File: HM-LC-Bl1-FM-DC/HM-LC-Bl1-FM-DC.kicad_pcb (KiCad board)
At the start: 2 copper layers, 53.1 x 26.9 mm, 32 parts, among them J2 FTDI, J4 Reset, K1 OMRONG6S-2, K2 OMRONG6S-2, Q1 BC817, Q2 BC817, SW2 Config, U1 ATMEGA328P-AU, U2 CC1101, U3 AM1S-2403S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

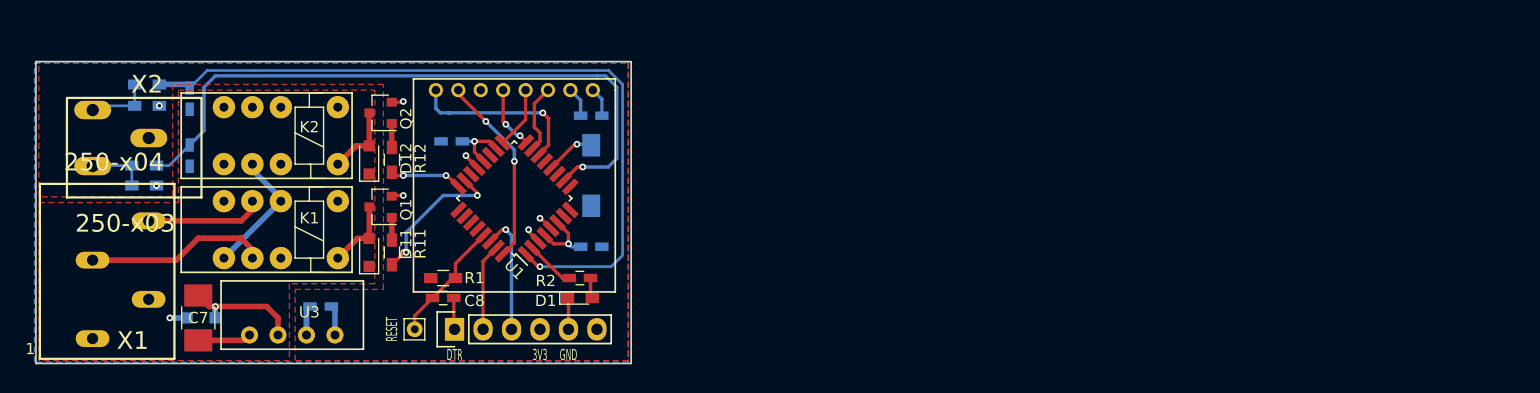
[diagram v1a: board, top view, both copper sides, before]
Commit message: basic routing finished
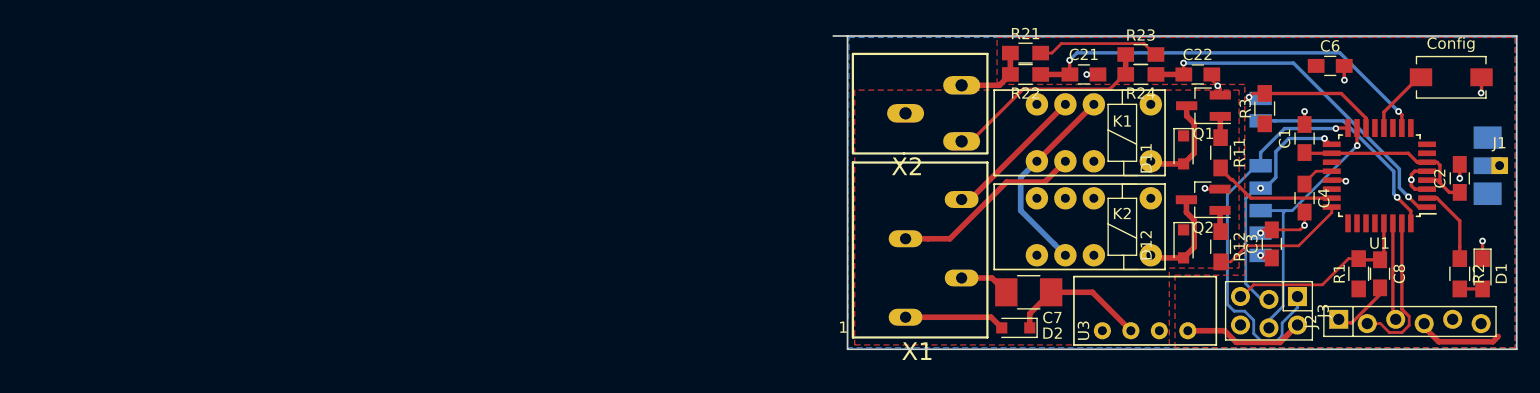
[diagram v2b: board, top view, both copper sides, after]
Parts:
- removed J4: Reset, Connectors:Pin_d0.7mm_L6.5mm_W1.8mm_FlatFork
- added C4: 100n, Capacitors_SMD:C_0805_HandSoldering, F.Cu at (181.1, 99.7)
- added J1: Conn_01x01, Measurement_Points:Measurement_Point_Square-TH_Small, F.Cu at (198.5, 96.8)
- added J3: ISP, myPinHeaders:Pin_Header_Straight_2x03_Pitch2.54mm_Tight_Fit, F.Cu at (180.5, 108.5)
- added R3: 10k, Resistors_SMD:R_0805_HandSoldering, F.Cu at (177.5, 91.7)
- C1, C2, C21, C22, C6: footprint Capacitors_SMD:C_0603_HandSoldering -> Capacitors_SMD:C_0805_HandSoldering; moved to F.Cu
- C3: value 100n -> 1u; footprint Capacitors_SMD:C_0603_HandSoldering -> Capacitors_SMD:C_0805_HandSoldering; moved to F.Cu
- C8: footprint Capacitors_SMD:C_0603_HandSoldering -> Capacitors_SMD:C_0805_HandSoldering
- D1: footprint LEDs:LED_0603_HandSoldering -> LEDs:LED_0805_HandSoldering
- D2, SW2: moved to F.Cu
- J2: value FTDI -> FtdiConnector; footprint Pin_Headers:Pin_Header_Straight_1x06 -> myPinHeaders:Pin_Header_Straight_1x06_Pitch2.54mm_Tight_Fit
- K1, K2: footprint Relay_mod:Relay_Omron_G6S-2 -> myRelais:Relay_Omron_G6S-2
- Q1, Q2: footprint TO_SOT_Packages_SMD:SOT-23 -> TO_SOT_Packages_SMD:SOT-23_Handsoldering
- R1, R11, R12: footprint Resistors_SMD:R_0603_HandSoldering -> Resistors_SMD:R_0805_HandSoldering
- R2: footprint Capacitors_SMD:C_0603_HandSoldering -> Resistors_SMD:R_0805_HandSoldering
- R21, R22, R23, R24: footprint Resistors_SMD:R_0603_HandSoldering -> Resistors_SMD:R_0805_HandSoldering; moved to F.Cu
- U1: value ATMEGA328P-AU -> ATmega328P-AU; footprint Housings_QFP:TQFP-32_7x7mm_Pitch0.8mm -> myHousings:TQFP-32_7x7mm_Pitch0.8mm_HandSoldering
- U2: footprint CC1101_Module:CC1101_Module -> myRadioModules:CC1101_SMD_noGDO2_Antenna; moved to B.Cu
- U3: footprint AM1S:SIL-4 -> myPowerModules:SIL-4
- X1: value 250-x04 -> ~
- X2: value 250-x03 -> ~
- moved C6 92.6 mm to (183.4, 87.9), turned to 0 degrees
- moved C22 89.9 mm to (171.6, 88.6), turned to 0 degrees
- moved R23 88.8 mm to (166.5, 86.9)
- moved R24 88.7 mm to (166.5, 88.6)
- moved J2 85.2 mm to (190.5, 110.7)
- moved C8 83.6 mm to (187.8, 106.4), turned to 270 degrees
- moved R1 81.7 mm to (185.9, 106.4), turned to 90 degrees
- moved D1 80.5 mm to (197.0, 106.4), turned to 270 degrees
- moved C21 80.1 mm to (161.4, 88.6), turned to 0 degrees
- moved R21 79.5 mm to (156.2, 86.7)
- moved R22 79.0 mm to (156.2, 88.6)
- moved R2 78.5 mm to (194.9, 106.4), turned to 270 degrees
- moved C2 77.7 mm to (194.9, 97.9), turned to 90 degrees
- moved SW2 77.2 mm to (194.2, 88.9), turned to 180 degrees
- moved U1 77.2 mm to (187.8, 97.7), turned to 180 degrees
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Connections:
- net /C0 renamed /REL_POL
- net /C1 renamed /REL_ON
- net /RXD renamed /RX
- net /TXD renamed /TX
- net Net-(R2-Pad1) renamed /LED
- net Net-(SW2-Pad2) renamed /CONFIG
- net Net-(U1-Pad14) renamed /CS
- net Net-(U1-Pad32) renamed /GDO0
- C21 pad 1: /D6 -> /UP
- C22 pad 1: /D3 -> /DOWN
- C8 pad 1: /DTR -> /RESET
- C8 pad 2: /Reset -> /DTR
- K2 pad 10: Net-(K2-Pad10) -> (no net)
- K2 pad 3: Net-(K2-Pad3) -> (no net)
- K2 pad 4: Net-(K2-Pad4) -> (no net)
- K2 pad 5: Net-(K2-Pad5) -> (no net)
- R1 pad 2: /Reset -> /RESET
- R21 pad 1: /UP -> /BUTTON_UP
- R22 pad 1: /D6 -> /UP
- R22 pad 2: /UP -> /BUTTON_UP
- R23 pad 1: /DOWN -> /BUTTON_DOWN
- R24 pad 1: /D3 -> /DOWN
- R24 pad 2: /DOWN -> /BUTTON_DOWN
- U1 pad 1: /D3 -> /DOWN
- U1 pad 10: /D6 -> /UP
- U1 pad 11: Net-(U1-Pad11) -> (no net)
- U1 pad 13: Net-(U1-Pad13) -> (no net)
- U1 pad 19: Net-(U1-Pad19) -> (no net)
- U1 pad 20: VCC -> Net-(C4-Pad1)
- U1 pad 22: Net-(U1-Pad22) -> (no net)
- U1 pad 25: Net-(U1-Pad25) -> (no net)
- U1 pad 26: Net-(U1-Pad26) -> (no net)
- U1 pad 27: Net-(U1-Pad27) -> (no net)
- U1 pad 28: Net-(U1-Pad28) -> (no net)
- U1 pad 29: /Reset -> /RESET
- U1 pad 7: Net-(U1-Pad7) -> (no net)
- U1 pad 8: Net-(U1-Pad8) -> (no net)
- U1 pad 9: Net-(U1-Pad9) -> (no net)
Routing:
- net /D3: track 67.6 -> 0.00 mm, vias 1 -> 0
- net /D6: track 59.0 -> 0.00 mm, vias 1 -> 0
- net /UP: track 5.29 -> 37.3 mm, vias 0 -> 2
- net VCC: track 16.8 -> 47.8 mm, vias 4 -> 1
- net /MISO: track 5.68 -> 34.9 mm, vias 2 -> 1
- net /DOWN: track 5.81 -> 31.5 mm, vias 0 -> 2
- net /BUTTON_DOWN: track 0.00 -> 18.9 mm
- net /MOSI: track 6.24 -> 23.8 mm, vias 0 -> 1
- net /RESET: track 0.00 -> 17.3 mm
- net /SCK: track 5.51 -> 21.8 mm, vias 0 -> 2
- net /Reset: track 11.3 -> 0.00 mm
- net +24V: track 1.54 -> 8.97 mm, vias 1 -> 0
- net GND: track 19.6 -> 26.3 mm, vias 5 -> 12
- net /BUTTON_UP: track 0.00 -> 6.65 mm
- net Net-(K1-Pad3): track 11.5 -> 17.8 mm
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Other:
- board size 53.1 x 26.9 mm -> 61 x 27.9 mm
- net class thick added: clearance 0.3, trace_width 0.5, via_dia 0.6, via_drill 0.3
- board text removed: "3V3"
- board text removed: "Config"
- board text removed: "DTR"
- board text removed: "GND"
- board text removed: "RESET"

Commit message: HM-LC-Bl1-FM-DC V3.0
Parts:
- C7: footprint Capacitors_SMD:C_1210_HandSoldering -> Capacitors_Tantalum_SMD:CP_Tantalum_Case-C_EIA-6032-28_Reflow
- D1: value LED_Rot -> LED
- J2: value FtdiConnector -> FTDI
- moved D2 2.28 mm to (157.6, 111.5)
- moved U3 1.14 mm to (161.7, 112.8)
- moved J2 0.89 mm to (191.4, 110.6)
- moved J3 0.89 mm to (181.4, 108.5)
- moved C7 0.82 mm to (157.2, 108.5)
- moved R23 0.13 mm to (166.5, 86.7)
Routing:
- net VCC: track 47.8 -> 54.0 mm
- net +24V: track 8.97 -> 11.3 mm
- net Net-(C7-Pad1): track 12.5 -> 11.4 mm
- net /RESET: track 17.3 -> 16.4 mm
- net /DTR: track 5.33 -> 4.81 mm
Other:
- board size 61 x 27.9 mm -> 59.7 x 27.9 mm
- board text added: "12V 24V"
- board text added: "DOWN"
- board text added: "GND"
- board text added: "HM-LC-Bl1-FM-DC stan23 V3.0 7/20"
- board text added: "M1"
- board text added: "M2"
- board text added: "UP"
- board text removed: "HM-LC-Bl1-FM-DC stan23 V2.1 10/18"
